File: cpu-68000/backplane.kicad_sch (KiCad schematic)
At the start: 29 parts, among them J201 Conn_03x32_Row_Letter_First, U201 SN74LVCH16T245, U202 SN74LVCH16T245, U203 SN74LXC8T245, U206 SN74LXC8T245

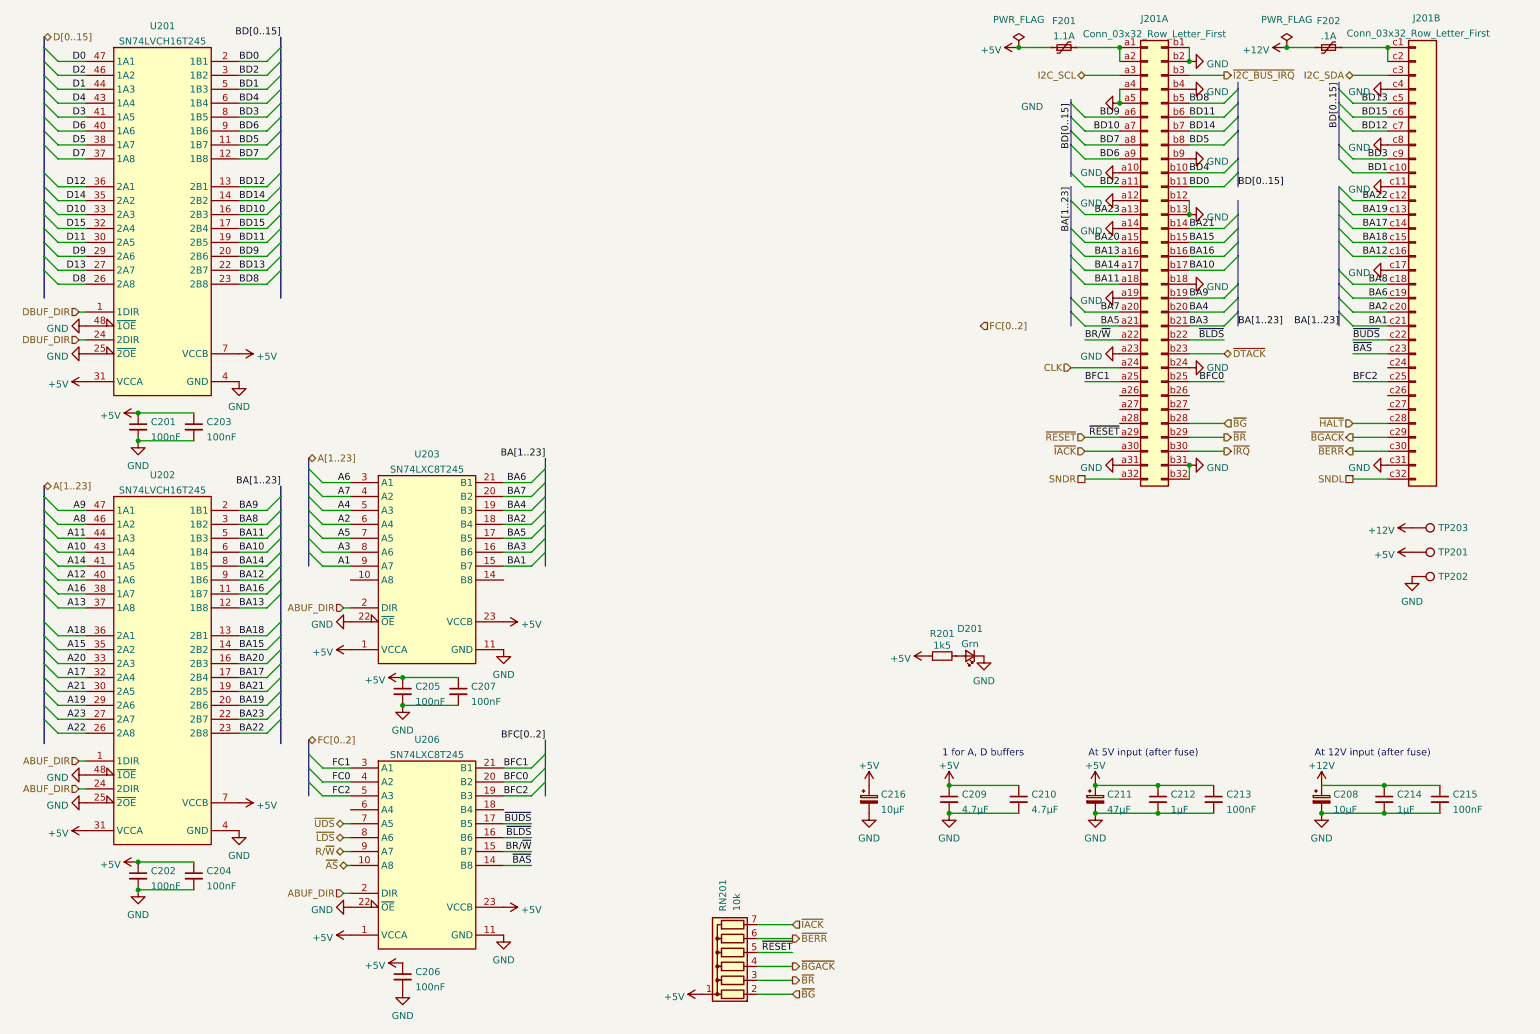
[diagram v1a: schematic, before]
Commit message: Schematic cleanup and ERC fixes
- Fixed many errors about duplicate or unassigned pins, and fixed some
  of the symbols and their pins directions.

- More minor tweaks to the pcb.
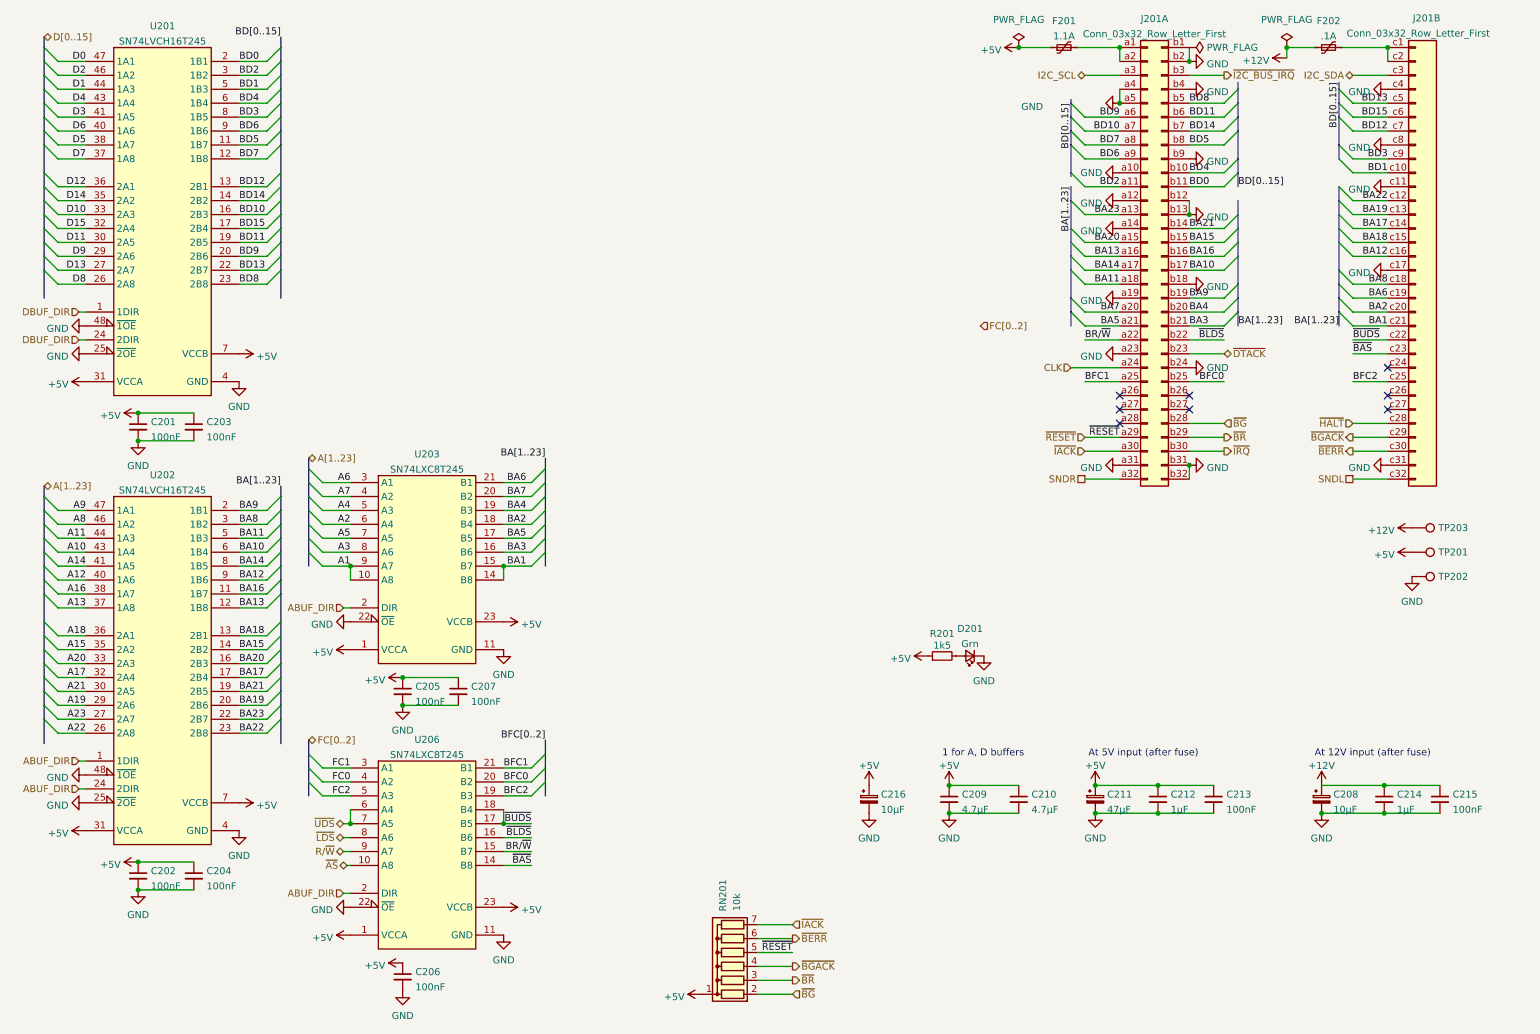
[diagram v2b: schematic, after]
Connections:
- net A1: now also U203.10 (A8)
- net BA1: now also U203.14 (B8)
- net ~{BUDS}: now also U206.18 (B4)
- net ~{UDS}: now also U206.6 (A4)
- no-connect marks 0 -> 8
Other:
- company: (none) -> Tristan Seifert
- title: (none) -> 68komputer CPU Board
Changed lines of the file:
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@@
 (kicad_sch (version 20211123) (generator eeschema)
   (paper "A4")
+  (title_block
+    (title "68komputer CPU Board")
+    (date "2021-12-11")
+    (rev "1")
+    (company "Tristan Seifert")
+  )
+  (junction (at 102.87 160.655) (diameter 0) (color 0 0 0 0)
+  )
   (junction (at 36.195 85.725) (diameter 0) (color 0 0 0 0)
   )
@@
   (junction (at 264.16 19.05) (diameter 0) (color 0 0 0 0)
   )
+  (junction (at 245.745 19.05) (diameter 0) (color 0 0 0 0)
+  )
   (junction (at 222.25 153.67) (diameter 0) (color 0 0 0 0)
   )
@@
   (junction (at 84.455 133.985) (diameter 0) (color 0 0 0 0)
   )
+  (junction (at 102.87 113.665) (diameter 0) (color 0 0 0 0)
+  )
+  (junction (at 74.93 113.665) (diameter 0) (color 0 0 0 0)
+  )
   (junction (at 84.455 139.065) (diameter 0) (color 0 0 0 0)
   )
+  (junction (at 74.93 160.655) (diameter 0) (color 0 0 0 0)
+  )
   (junction (at 210.82 158.75) (diameter 0) (color 0 0 0 0)
   )
   (junction (at 222.25 158.75) (diameter 0) (color 0 0 0 0)
   )
-  (junction (at 245.745 19.05) (diameter 0) (color 0 0 0 0)
-  )
   (junction (at 210.82 153.67) (diameter 0) (color 0 0 0 0)
   )
+  (no_connect (at 227.965 82.55))
+  (no_connect (at 227.965 85.09))
+  (no_connect (at 264.16 77.47))
+  (no_connect (at 264.16 82.55))
+  (no_connect (at 264.16 85.09))
+  (no_connect (at 215.265 82.55))
+  (no_connect (at 215.265 87.63))
+  (no_connect (at 215.265 85.09))
   (bus_entry (at 206.375 57.15) (size 2.54 2.54)
     (stroke (width 0) (type default) (color 0 0 0 0))
@@
     (stroke (width 0) (type default) (color 0 0 0 0))
   )
+  (wire (pts (xy 102.87 158.115) (xy 102.87 160.655))
+    (stroke (width 0) (type default) (color 0 0 0 0))
+  )
   (wire (pts (xy 69.85 106.045) (xy 74.93 106.045))
     (stroke (width 0) (type default) (color 0 0 0 0))
@@
     (stroke (width 0) (type default) (color 0 0 0 0))
   )
+  (wire (pts (xy 74.93 158.115) (xy 74.93 160.655))
+    (stroke (width 0) (type default) (color 0 0 0 0))
+  )
   (wire (pts (xy 54.61 141.605) (xy 59.69 141.605))
     (stroke (width 0) (type default) (color 0 0 0 0))
@@
     (stroke (width 0) (type default) (color 0 0 0 0))
   )
+  (wire (pts (xy 102.87 113.665) (xy 102.87 116.205))
+    (stroke (width 0) (type default) (color 0 0 0 0))
+  )
   (wire (pts (xy 215.265 19.05) (xy 215.265 21.59))
     (stroke (width 0) (type default) (color 0 0 0 0))
@@
     (stroke (width 0) (type default) (color 0 0 0 0))
   )
+  (wire (pts (xy 245.745 19.05) (xy 245.745 20.955))
+    (stroke (width 0) (type default) (color 0 0 0 0))
+  )
   (wire (pts (xy 208.915 80.01) (xy 215.265 80.01))
     (stroke (width 0) (type default) (color 0 0 0 0))
@@
   )
   (bus (pts (xy 206.375 28.575) (xy 206.375 29.21))
+    (stroke (width 0) (type default) (color 0 0 0 0))
+  )
+  (wire (pts (xy 74.93 113.665) (xy 74.93 116.205))
     (stroke (width 0) (type default) (color 0 0 0 0))
   )
@@
     (pin "9")
   )
-  (symbol (lib_id "power:+12V") (at 245.745 19.05 90) (unit 1)
-    (in_bom yes) (on_board yes) (fields_autoplaced)
-    (property "Reference" "#PWR0264" (id 0) (at 249.555 19.05 0)
-      (effects (font (size 1.27 1.27)) hide)
-    )
-    (property "Value" "+12V" (id 1) (at 242.57 19.529 90)
+  (symbol (lib_id "power:+12V") (at 245.745 20.955 90) (unit 1)
+    (in_bom yes) (on_board yes) (fields_autoplaced)
+    (property "Reference" "#PWR0264" (id 0) (at 249.555 20.955 0)
+      (effects (font (size 1.27 1.27)) hide)
+    )
+    (property "Value" "+12V" (id 1) (at 242.57 21.434 90)
       (effects (font (size 1.27 1.27)) (justify left))
     )
-    (property "Footprint" "" (id 2) (at 245.745 19.05 0)
-      (effects (font (size 1.27 1.27)) hide)
-    )
-    (property "Datasheet" "" (id 3) (at 245.745 19.05 0)
+    (property "Footprint" "" (id 2) (at 245.745 20.955 0)
+      (effects (font (size 1.27 1.27)) hide)
+    )
+    (property "Datasheet" "" (id 3) (at 245.745 20.955 0)
       (effects (font (size 1.27 1.27)) hide)
     )
@@
       (effects (font (size 1.27 1.27)) hide)
     )
+    (pin "1")
+  )
+  (symbol (lib_id "power:PWR_FLAG") (at 227.965 19.05 270) (unit 1)
+    (in_bom yes) (on_board yes) (fields_autoplaced)
+    (property "Reference" "#FLG0103" (id 0) (at 229.87 19.05 0)
+      (effects (font (size 1.27 1.27)) hide)
+    )
+    (property "Value" "PWR_FLAG" (id 1) (at 231.14 19.0499 90)
+      (effects (font (size 1.27 1.27)) (justify left))
+    )
+    (property "Footprint" "" (id 2) (at 227.965 19.05 0)
+      (effects (font (size 1.27 1.27)) hide)
+    )
+    (property "Datasheet" "~" (id 3) (at 227.965 19.05 0)
+      (effects (font (size 1.27 1.27)) hide)
+    )

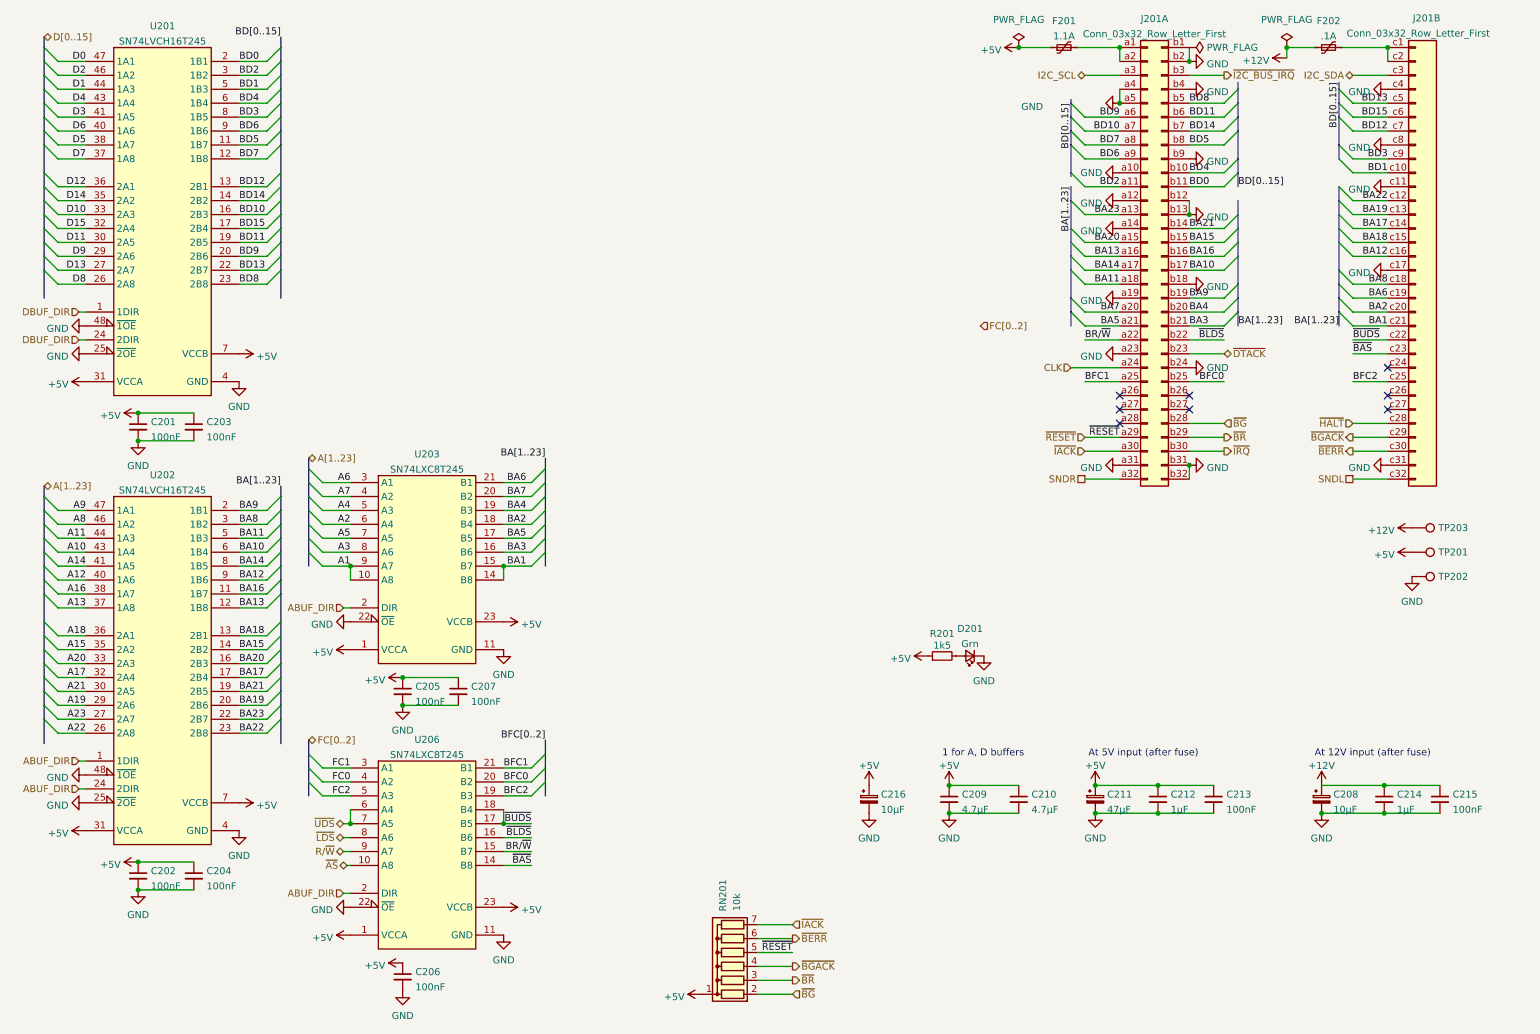
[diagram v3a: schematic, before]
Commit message: Start of rev 2 board
- This drops bus buffers, and replaces flash with DIP socketed versions.
  Also some minor tweaks to the board

- Fixed power LED (D201) positioning

- Fixed LED (too dark) for the right angle indicators
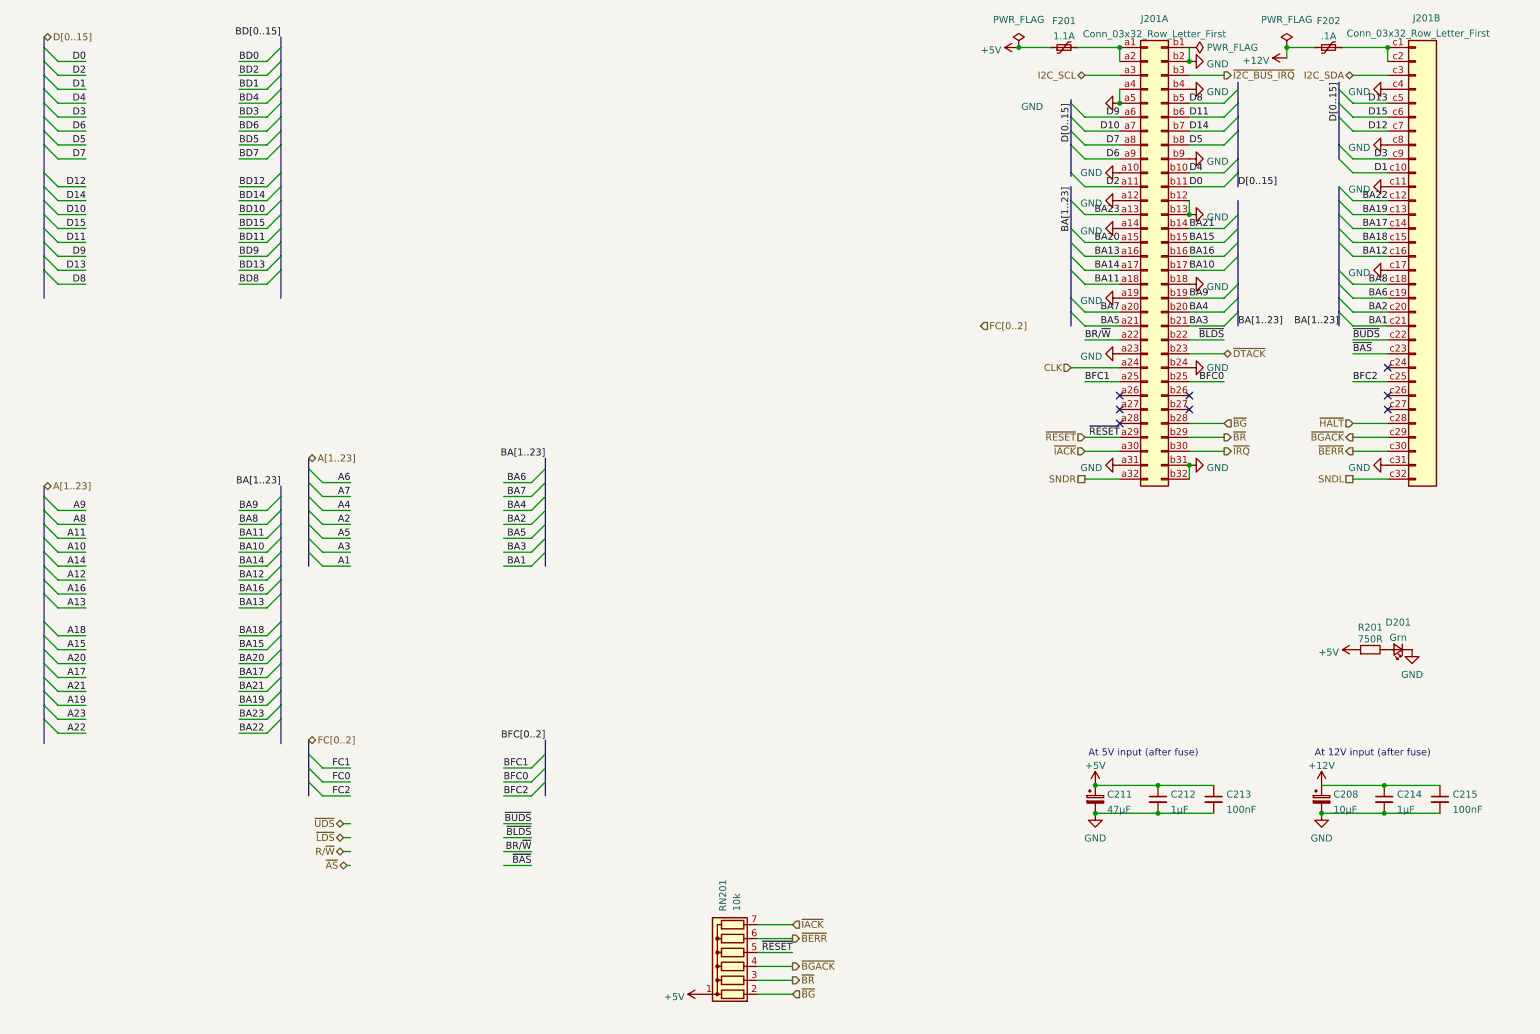
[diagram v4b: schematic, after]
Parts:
- removed C201, C202, C203, C204, C205, C206, C207: 100nF, Capacitor_SMD:C_0805_2012Metric, symbol Device:C_Small
- removed C209, C210: 4.7µF, Capacitor_SMD:C_0805_2012Metric, symbol Device:C_Small
- removed C216: 10µF, Capacitor_Tantalum_SMD:CP_EIA-3216-18_Kemet-A, symbol Device:C_Polarized_Small
- removed TP201, TP202, TP203: TestPoint, TestPoint:TestPoint_Loop_D2.60mm_Drill1.4mm_Beaded, symbol Connector:TestPoint
- removed U201, U202: SN74LVCH16T245, Package_SO:TSSOP-48_6.1x12.5mm_P0.5mm, symbol 68komputer-common:SN74LVCH16T245
- removed U203, U206: SN74LXC8T245, Package_SO:TSSOP-24_4.4x7.8mm_P0.65mm, symbol 68komputer-common:SN74LXC8T245
- R201: value 1k5 -> 750R
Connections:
- net BD0: no longer J201.b11 (Pin_b11)
- net BD1: no longer J201.c10 (Pin_c10)
- net BD10: no longer J201.a7 (Pin_a7)
- net BD11: no longer J201.b6 (Pin_b6)
- net BD12: no longer J201.c7 (Pin_c7)
- net BD13: no longer J201.c5 (Pin_c5)
- net BD14: no longer J201.b7 (Pin_b7)
- net BD15: no longer J201.c6 (Pin_c6)
- net BD2: no longer J201.a11 (Pin_a11)
- net BD3: no longer J201.c9 (Pin_c9)
- net BD4: no longer J201.b10 (Pin_b10)
- net BD5: no longer J201.b8 (Pin_b8)
- net BD6: no longer J201.a9 (Pin_a9)
- net BD7: no longer J201.a8 (Pin_a8)
- net BD8: no longer J201.b5 (Pin_b5)
- net BD9: no longer J201.a6 (Pin_a6)
- net D0: now also J201.b11 (Pin_b11)
- net D1: now also J201.c10 (Pin_c10)
- net D10: now also J201.a7 (Pin_a7)
- net D11: now also J201.b6 (Pin_b6)
- net D12: now also J201.c7 (Pin_c7)
- net D13: now also J201.c5 (Pin_c5)
- net D14: now also J201.b7 (Pin_b7)
- net D15: now also J201.c6 (Pin_c6)
- net D2: now also J201.a11 (Pin_a11)
- net D3: now also J201.c9 (Pin_c9)
- net D4: now also J201.b10 (Pin_b10)
- net D5: now also J201.b8 (Pin_b8)
- net D6: now also J201.a9 (Pin_a9)
- net D7: now also J201.a8 (Pin_a8)
- net D8: now also J201.b5 (Pin_b5)
- net D9: now also J201.a6 (Pin_a6)
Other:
- note removed: "1 for A, D buffers"
- moved on the sheet: D201, R201
